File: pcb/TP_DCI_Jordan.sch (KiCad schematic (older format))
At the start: 19 parts, among them J1 MICRO, J2 Display, SW1 SW_DIP_x03, U1 PCF8574

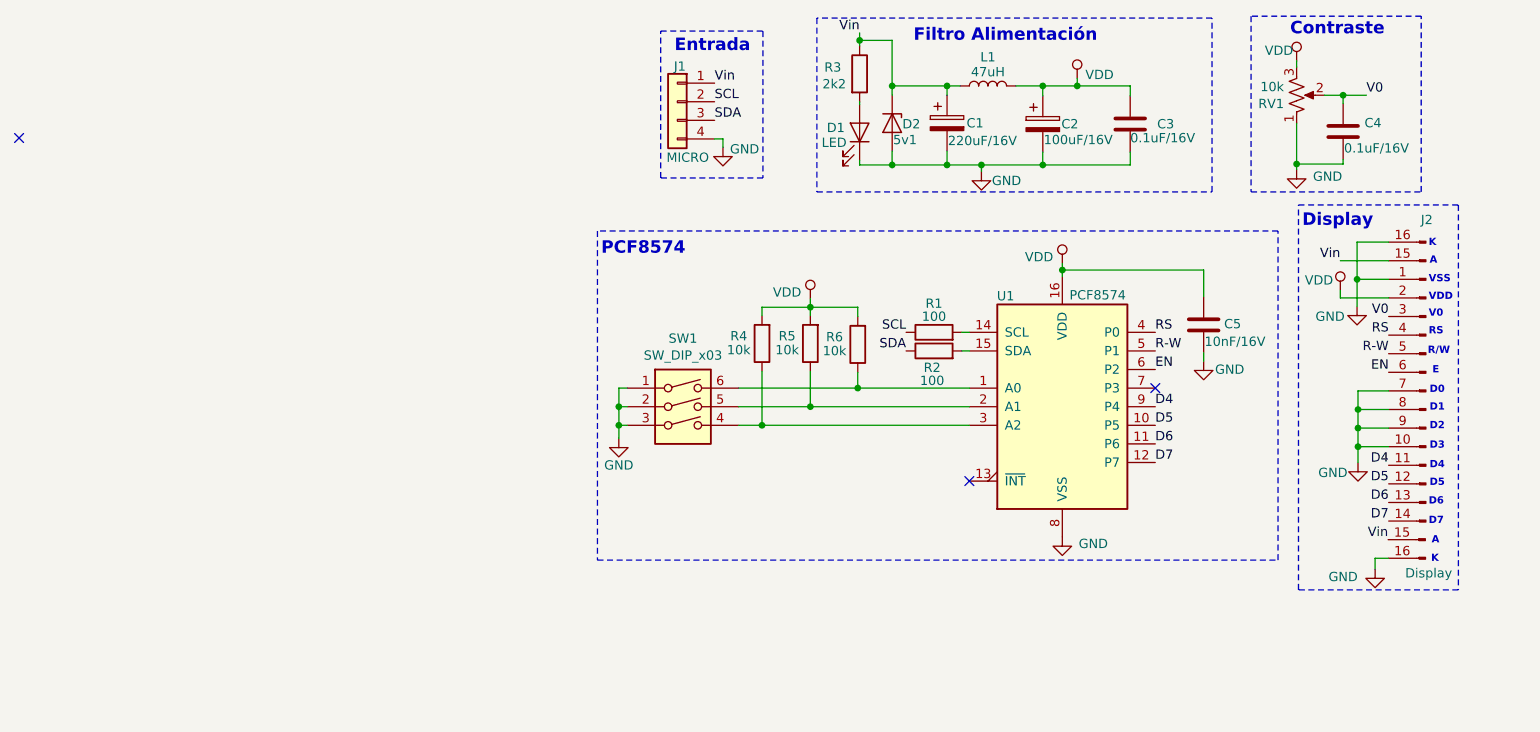
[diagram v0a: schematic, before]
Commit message: agregado de PWR flags, cero errores ERC
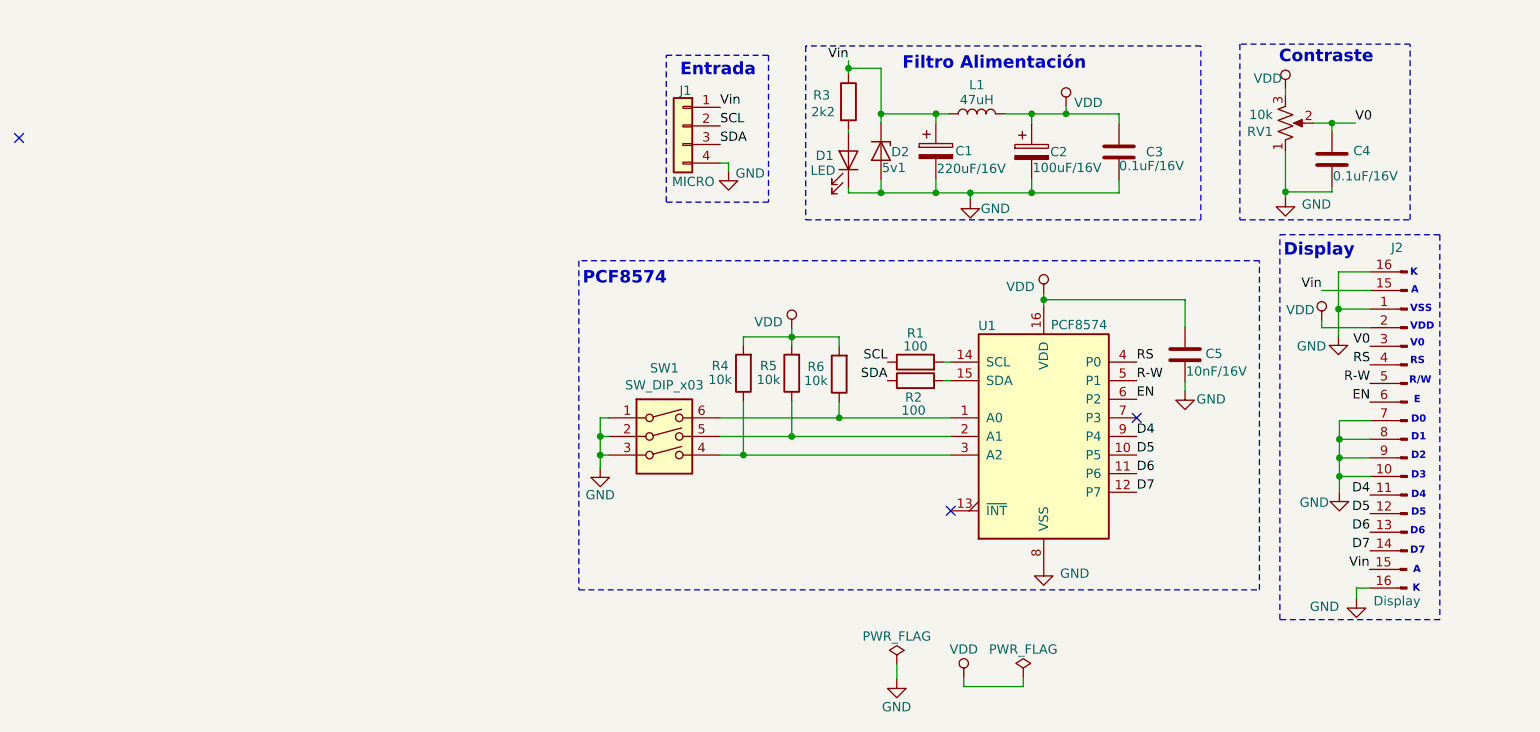
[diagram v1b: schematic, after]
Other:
- moved on the sheet: C1, C2, C3, C4, C5, D1, D2, J1, J2, L1, R1, R2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

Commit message: Comentarios en bloques
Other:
- note added: "Eliminación de Rpu y agregado de Rserie,\nrespecto de módulos comerciales."
- note added: "Se adapta a varios tipos \nde Displays de 16 pines, \nmediante 18 pines de salida."
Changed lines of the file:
@@
 Comp ""
 Comment1 "Autor: Jordán Joan Emmanuel"
-Comment2 "Proyecto bajo licencia CERN Open Hardware Licence V2"
+Comment2 "Bajo licencia CERN Open Hardware Licence V2. Basado en réplica LCD-i2c comercial"
 Comment3 "Diseño de Circuitos Impresos - Carrera de Especialización en Sistemas Embebidos"
 Comment4 "Facultad de Ingeniería de la Universidad de Buenos Aires"
@@
 P 4410 5805
 F 0 "U1" H 4105 6400 50  0000 C CNN
-F 1 "PCF8574" H 4600 6405 50  0000 C CNN
+F 1 "PCF8574" H 4760 5210 50  0000 C CNN
 F 2 "miSMD:SOIC127P1030X265-16N" H 4410 5805 50  0001 C CNN
 F 3 "http://www.nxp.com/documents/data_sheet/PCF8574_PCF8574A.pdf" H 4410 5805 50  0001 C CNN
@@
 Wire Wire Line
 	4300 7150 4300 7100
+Text Notes 5640 7060 0    50   ~ 0
+Se adapta a varios tipos \nde Displays de 16 pines, \nmediante 18 pines de salida.
+Text Notes 2180 6430 0    50   ~ 0
+Eliminación de Rpu y agregado de Rserie,\nrespecto de módulos comerciales.
 $EndSCHEMATC
